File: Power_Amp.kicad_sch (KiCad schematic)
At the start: 20 parts, among them J87 Molex 73251-1153, U86 TQP7M9106

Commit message: Lots of notes and things about various items
Signed-off-by: Corey Minyard <corey@minyard.net>
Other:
- note added: "-1.3 dB"
- note added: "DC bias may affect the value of this capacitor. May need to adjust."
- note added: "Output impedance is 6.23 - j13.3 ohms This converts to 50 ohms at 435MHz"
- note added: "Place by the PA."
- note removed: "Place by the CPU."
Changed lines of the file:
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@@
 		)
 	)
-	(text "Place by the CPU."
+	(text "Place by the PA."
 		(exclude_from_sim no)
 		(at 302.514 127.254 0)
@@
 		)
 	)
+	(text "-1.3 dB"
+		(exclude_from_sim no)
+		(at 291.084 181.61 0)
+		(effects
+			(font
+				(size 1.524 1.524)
+			)
+			(justify left bottom)
+		)
+	)
 	(text "Symbol Numbers 700 up"
 		(exclude_from_sim no)
@@
 		)
 	)
+	(text "DC bias may affect the\nvalue of this capacitor.\nMay need to adjust."
+		(exclude_from_sim no)
+		(at 227.584 151.13 0)
+		(effects
+			(font
+				(size 1.524 1.524)
+			)
+		)
+	)
 	(text "Connect External 2.7 VDC supply\nhere for testing."
 		(exclude_from_sim no)
@@
 			)
 			(justify left bottom)
+		)
+	)
+	(text "Output impedance is\n6.23 - j13.3 ohms\nThis converts to 50 ohms\nat 435MHz"
+		(exclude_from_sim no)
+		(at 210.566 171.196 0)
+		(effects
+			(font
+				(size 1.524 1.524)
+			)
 		)
 	)
@@
 		(dnp no)
 		(property "Reference" "L707"
-			(at 198.12 138.43 0)
+			(at 196.342 140.97 90)
 			(effects
 				(font
@@
 		)
 		(property "Value" "18n"
-			(at 189.23 138.43 0)
-			(effects
-				(font
+			(at 191.77 140.716 90)
+			(effects
+				(font

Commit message: Add shields around AX5043s, replace UFL connectors
Signed-off-by: Corey Minyard <corey@minyard.net>
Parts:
- P701: value ~ -> CONUFL001-SMD-T; footprint PacSatDev_misc:U_FL -> PacSatDev_misc:CONN1_CONUFL_TEC
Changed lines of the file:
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@@
 			)
 		)
-		(property "Value" "~"
+		(property "Value" "CONUFL001-SMD-T"
 			(at 55.88 113.03 0)
 			(effects
@@
 					(size 1.27 1.27)
 				)
+				(hide yes)
 			)
 		)
-		(property "Footprint" "PacSatDev_misc:U_FL"
+		(property "Footprint" "PacSatDev_misc:CONN1_CONUFL_TEC"
 			(at 55.88 113.03 0)
 			(effects

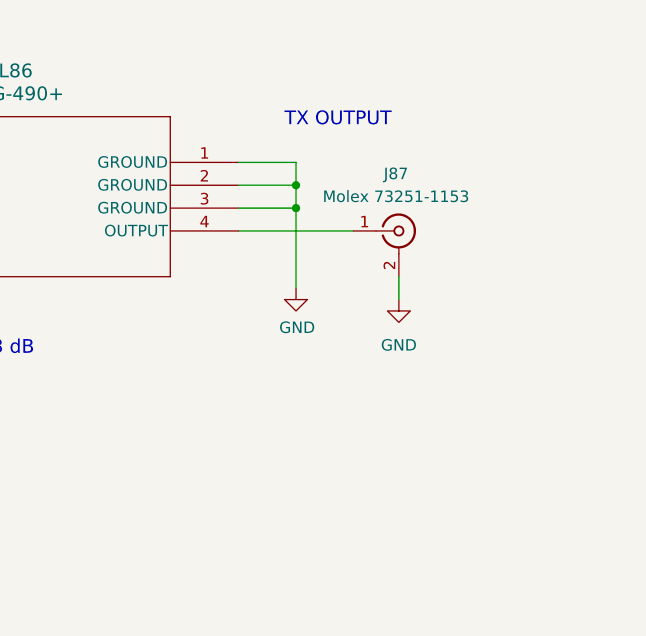
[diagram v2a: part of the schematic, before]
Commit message: Set orientaion of the shields, add bleed off inductor to TX
Signed-off-by: Corey Minyard <corey@minyard.net>
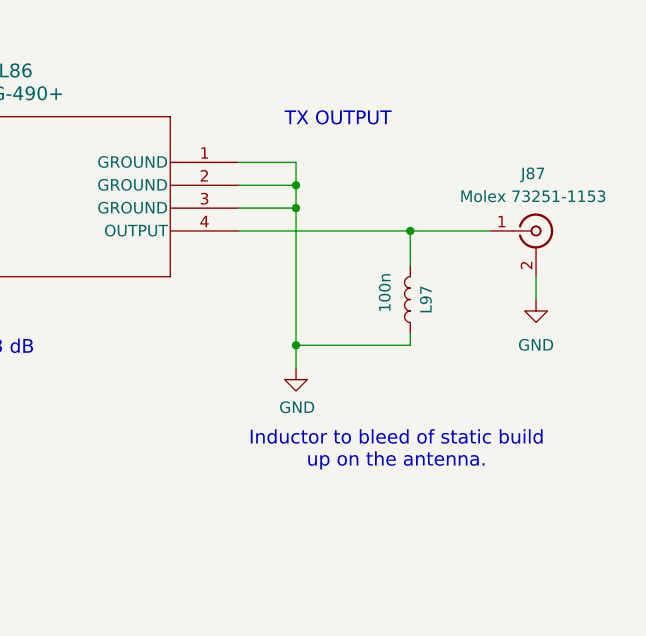
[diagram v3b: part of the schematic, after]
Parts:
- added L97: 100n, Inductor_SMD:L_0603_1608Metric_Pad1.05x0.95mm_HandSolder, symbol Device:L
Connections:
- net GND: now also L97.1
- net at FL86.4 (OUTPUT), J87.1 (In): now also L97.2
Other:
- note added: "Inductor to bleed of static build up on the antenna."
- moved on the sheet: J87
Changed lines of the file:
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@@
 		(comment 1 "N5BRG")
+	)
+	(text "Inductor to bleed of static build\nup on the antenna."
+		(exclude_from_sim no)
+		(at 338.836 192.024 0)
+		(effects
+			(font
+				(size 1.524 1.524)
+			)
+		)
 	)
 	(text "Adjust Voltage and Current for 2W"
@@
 	)
 	(junction
+		(at 327.66 180.34)
+		(diameter 0)
+		(color 0 0 0 0)
+	)
+	(junction
 		(at 147.32 149.86)
 		(diameter 0)
@@
 	)
 	(junction
+		(at 340.36 167.64)
+		(diameter 0)
+		(color 0 0 0 0)
+	)
+	(junction
 		(at 83.82 149.86)
 		(diameter 0)
@@
 	(wire
 		(pts
+			(xy 327.66 180.34) (xy 327.66 182.88)
+		)
+		(stroke
+			(width 0)
+			(type default)
+		)
+	)
+	(wire
+		(pts
 			(xy 83.82 149.86) (xy 90.17 149.86)
 		)
@@
 	(wire
 		(pts
+			(xy 340.36 180.34) (xy 327.66 180.34)
+		)
+		(stroke
+			(width 0)
+			(type default)
+		)
+	)
+	(wire
+		(pts
 			(xy 267.97 162.56) (xy 267.97 165.1)
 		)
@@
 	(wire
 		(pts
+			(xy 340.36 167.64) (xy 321.31 167.64)
+		)
+		(stroke
+			(width 0)
+			(type default)
+		)
+	)
+	(wire
+		(pts
 			(xy 194.31 116.84) (xy 194.31 128.27)
 		)
@@
 	(wire
 		(pts
-			(xy 334.01 167.64) (xy 321.31 167.64)
+			(xy 349.25 167.64) (xy 340.36 167.64)
 		)
 		(stroke
@@
 	(wire
 		(pts
-			(xy 339.09 172.72) (xy 339.09 175.26)
-		)
-		(stroke
-			(width 0)
-			(type default)
-		)
-	)
-	(wire
-		(pts
-			(xy 327.66 165.1) (xy 327.66 173.99)
+			(xy 354.33 172.72) (xy 354.33 175.26)
+		)
+		(stroke
+			(width 0)
+			(type default)
+		)
+	)
+	(wire
+		(pts
+			(xy 327.66 165.1) (xy 327.66 180.34)
 		)
 		(stroke
@@
 	(wire
 		(pts
+			(xy 340.36 167.64) (xy 340.36 171.45)
+		)
+		(stroke
+			(width 0)
+			(type default)
+		)
+	)
+	(wire
+		(pts
 			(xy 218.44 160.02) (xy 194.31 160.02)
 		)
@@
 		(pts
 			(xy 52.07 113.03) (xy 50.8 113.03)
+		)
+		(stroke
+			(width 0)
+			(type default)
+		)
+	)
+	(wire
+		(pts
+			(xy 340.36 179.07) (xy 340.36 180.34)
 		)
 		(stroke
@@
 	(symbol
 		(lib_id "Connector:Conn_Coaxial")
-		(at 339.09 167.64 0)
+		(at 354.33 167.64 0)
 		(unit 1)
 		(exclude_from_sim no)
@@
 		(fields_autoplaced yes)
 		(property "Reference" "J87"
-			(at 338.7726 161.29 0)
+			(at 354.0126 161.29 0)
 			(effects
 				(font
@@
 		)
 		(property "Value" "Molex 73251-1153"
-			(at 338.7726 163.83 0)
+			(at 354.0126 163.83 0)
 			(effects
 				(font
@@
 		)
 		(property "Footprint" "Connector_Coaxial:SMA_Molex_73251-1153_EdgeMount_Horizontal"
-			(at 339.09 167.64 0)
+			(at 354.33 167.64 0)
 			(effects
 				(font
@@
 		)
 		(property "Datasheet" "~"
-			(at 339.09 167.64 0)
+			(at 354.33 167.64 0)
 			(effects
 				(font
@@
 		)
 		(property "Description" "coaxial connector (BNC, SMA, SMB, SMC, Cinch/RCA, LEMO, ...)"
-			(at 339.09 167.64 0)
+			(at 354.33 167.64 0)
 			(effects
 				(font
@@
 	(symbol
 		(lib_id "power:GND")
-		(at 327.66 173.99 0)
+		(at 327.66 182.88 0)
 		(unit 1)
 		(exclude_from_sim no)
@@
 		(dnp no)
 		(property "Reference" "#PWR0200"
-			(at 327.66 180.34 0)
+			(at 327.66 189.23 0)
 			(effects
 				(font
@@
 		)
 		(property "Value" "GND"
-			(at 327.787 178.3842 0)
+			(at 327.787 187.2742 0)
 			(effects
 				(font
@@
 		)
 		(property "Footprint" ""
-			(at 327.66 173.99 0)
+			(at 327.66 182.88 0)
 			(effects
 				(font
@@
 		)
 		(property "Datasheet" ""
-			(at 327.66 173.99 0)
+			(at 327.66 182.88 0)
 			(effects
 				(font
@@
 		)
 		(property "Description" ""
-			(at 327.66 173.99 0)
+			(at 327.66 182.88 0)
 			(effects
 				(font
@@
 	(symbol
 		(lib_id "power:GND")
-		(at 339.09 175.26 0)
+		(at 354.33 175.26 0)
 		(mirror y)
 		(unit 1)
@@
 		(fields_autoplaced yes)
 		(property "Reference" "#PWR0191"
-			(at 339.09 181.61 0)
+			(at 354.33 181.61 0)
 			(effects
 				(font
@@
 		)
 		(property "Value" "GND"
-			(at 339.09 180.34 0)
+			(at 354.33 180.34 0)
 			(effects
 				(font
@@
 		)
 		(property "Footprint" ""
-			(at 339.09 175.26 0)
+			(at 354.33 175.26 0)
 			(effects
 				(font
@@
 		)
 		(property "Datasheet" ""
-			(at 339.09 175.26 0)
+			(at 354.33 175.26 0)
 			(effects
 				(font
@@
 		)
 		(property "Description" ""
-			(at 339.09 175.26 0)
+			(at 354.33 175.26 0)
 			(effects
 				(font
@@
 					(unit 1)
 				)
+			)
+		)
+	)
+	(symbol
+		(lib_id "Device:L")
+		(at 340.36 175.26 180)
+		(unit 1)
+		(exclude_from_sim no)
+		(in_bom yes)
+		(on_board yes)
+		(dnp no)
+		(property "Reference" "L97"
+			(at 342.138 175.26 90)
+			(effects
+				(font
+					(size 1.27 1.27)
+				)
+			)
+		)
+		(property "Value" "100n"
+			(at 337.566 174.498 90)
+			(effects
+				(font
+					(size 1.27 1.27)
+				)
+			)
+		)
+		(property "Footprint" "Inductor_SMD:L_0603_1608Metric_Pad1.05x0.95mm_HandSolder"
+			(at 340.36 175.26 0)
+			(effects
+				(font
+					(size 1.27 1.27)
+				)
+				(hide yes)
+			)
+		)
+		(property "Datasheet" "~"
+			(at 340.36 175.26 0)
+			(effects
+				(font
+					(size 1.27 1.27)
+				)
+				(hide yes)
+			)
+		)
+		(property "Description" ""
+			(at 340.36 175.26 0)
+			(effects
+				(font
+					(size 1.27 1.27)
+				)
+			)
+		)
+		(pin "1"
+		)
+		(pin "2"
+		)
+		(instances
+			(project "PacSat_AFSK"
+				(path "/cc9f42d2-6985-41ac-acab-5ab7b01c5b38/b85b88c3-87c5-49e2-804e-0759552ace3d"
+					(reference "L97")
+					(unit 1)
+				)

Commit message: Rework the AX5043 RX side to a different balun
It's cheaper (though not smaller) and fits inside the shield.

Signed-off-by: Corey Minyard <corey@minyard.net>
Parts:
- removed R133: 0, Resistor_SMD:R_0603_1608Metric_Pad0.98x0.95mm_HandSolder, symbol Device:R
- added C137: 100p, Capacitor_SMD:C_0603_1608Metric_Pad1.08x0.95mm_HandSolder, symbol Device:C
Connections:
- net TX_OUT_DRV: now also C137.1
- net at C708.1, L706.1, P701.1 (In): now also C137.2
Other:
- note removed: "Adjust Voltage and Current for 2W"
- note removed: "Connect External 2.7 VDC supply here for testing."
- note removed: "RF Shield over these parts."
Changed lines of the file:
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@@
 		)
 	)
-	(text "Adjust Voltage and Current for 2W"
-		(exclude_from_sim no)
-		(at 119.38 59.69 0)
-		(effects
-			(font
-				(size 1.524 1.524)
-			)
-			(justify right bottom)
-		)
-	)
 	(text "Place by the PA."
 		(exclude_from_sim no)
@@
 		)
 	)
-	(text "RF Shield over these parts."
-		(exclude_from_sim no)
-		(at 31.75 186.69 0)
-		(effects
-			(font
-				(size 1.524 1.524)
-			)
-			(justify left bottom)
-		)
-	)
 	(text "33 dBm\n2 W"
 		(exclude_from_sim no)
@@
 		)
 	)
-	(text "Connect External 2.7 VDC supply\nhere for testing."
-		(exclude_from_sim no)
-		(at 153.67 40.64 0)
-		(effects
-			(font
-				(size 1.524 1.524)
-			)
-			(justify right bottom)
-		)
-	)
 	(text "Input impedance is\n1.87 - 37.7j this\nmatches to 50 ohms\nat 435MHz."
 		(exclude_from_sim no)
@@
 	)
 	(symbol
-		(lib_id "Device:R")
-		(at 45.72 142.24 90)
-		(unit 1)
-		(exclude_from_sim no)
-		(in_bom yes)
-		(on_board yes)
-		(dnp no)
-		(fields_autoplaced yes)
-		(property "Reference" "R133"
-			(at 45.72 135.89 90)
-			(effects
-				(font
-					(size 1.27 1.27)
-				)
-			)
-		)
-		(property "Value" "0"
-			(at 45.72 138.43 90)
-			(effects
-				(font
-					(size 1.27 1.27)
-				)
-			)
-		)
-		(property "Footprint" "Resistor_SMD:R_0603_1608Metric_Pad0.98x0.95mm_HandSolder"
-			(at 45.72 144.018 90)
-			(effects
-				(font
-					(size 1.27 1.27)
-				)
-				(hide yes)
-			)
-		)
-		(property "Datasheet" "~"
-			(at 45.72 142.24 0)
-			(effects
-				(font
-					(size 1.27 1.27)
-				)
-				(hide yes)
-			)
-		)
-		(property "Description" ""
-			(at 45.72 142.24 0)
-			(effects
-				(font
-					(size 1.27 1.27)
-				)
-			)
-		)
-		(pin "1"
-		)
-		(pin "2"
-		)
-		(instances
-			(project "PacSat_AFSK"
-				(path "/cc9f42d2-6985-41ac-acab-5ab7b01c5b38/b85b88c3-87c5-49e2-804e-0759552ace3d"
-					(reference "R133")
-					(unit 1)
-				)
-			)
-		)
-	)
-	(symbol
 		(lib_id "power:GND")
 		(at 327.66 182.88 0)
@@
 					(unit 1)
 				)
+			)
+		)
+	)
+	(symbol
+		(lib_id "Device:C")
+		(at 45.72 142.24 90)
+		(mirror x)
+		(unit 1)
+		(exclude_from_sim no)
+		(in_bom yes)
+		(on_board yes)
+		(dnp no)
+		(property "Reference" "C137"
+			(at 45.72 135.89 90)
+			(effects
+				(font
+					(size 1.27 1.27)
+				)
+			)
+		)
+		(property "Value" "100p"
+			(at 45.72 138.43 90)
+			(effects
+				(font
+					(size 1.27 1.27)
+				)
+			)
+		)
+		(property "Footprint" "Capacitor_SMD:C_0603_1608Metric_Pad1.08x0.95mm_HandSolder"
+			(at 49.53 143.2052 0)
+			(effects
+				(font
+					(size 1.27 1.27)
+				)
+				(hide yes)
+			)
+		)
+		(property "Datasheet" "~"
+			(at 45.72 142.24 0)
+			(effects
+				(font
+					(size 1.27 1.27)
+				)
+				(hide yes)
+			)
+		)
+		(property "Description" ""
+			(at 45.72 142.24 0)
+			(effects
+				(font
+					(size 1.27 1.27)
+				)
+			)
+		)
+		(pin "1"
+		)
+		(pin "2"
+		)
+		(instances
+			(project "PacSat_AFSK"
+				(path "/cc9f42d2-6985-41ac-acab-5ab7b01c5b38/b85b88c3-87c5-49e2-804e-0759552ace3d"
+					(reference "C137")
+					(unit 1)
+				)

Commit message: Add shield for the TX PA section
Signed-off-by: Corey Minyard <corey@minyard.net>
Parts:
- added J94: PIC-S-203F, PacSatDev_misc:RF_SHIELD_PIC_S_203, symbol Device:RFShield_OnePiece
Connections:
- net GND: now also J94.1 (Shield)
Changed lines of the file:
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@@
+	(wire
+		(pts
+			(xy 105.41 58.42) (xy 105.41 60.96)
+		)
+		(stroke
+			(width 0)
+			(type default)
+		)
+	)
 	(wire
 		(pts
@@
 				(path "/cc9f42d2-6985-41ac-acab-5ab7b01c5b38/b85b88c3-87c5-49e2-804e-0759552ace3d"
 					(reference "P701")
+					(unit 1)
+				)
+			)
+		)
+	)
+	(symbol
+		(lib_id "Device:RFShield_OnePiece")
+		(at 105.41 48.26 0)
+		(unit 1)
+		(exclude_from_sim no)
+		(in_bom yes)
+		(on_board yes)
+		(dnp no)
+		(fields_autoplaced yes)
+		(property "Reference" "J94"
+			(at 121.92 46.9899 0)
+			(effects
+				(font
+					(size 1.27 1.27)
+				)
+				(justify left)
+			)
+		)
+		(property "Value" "PIC-S-203F"
+			(at 121.92 49.5299 0)
+			(effects
+				(font
+					(size 1.27 1.27)
+				)
+				(justify left)
+			)
+		)
+		(property "Footprint" "PacSatDev_misc:RF_SHIELD_PIC_S_203"
+			(at 105.41 50.8 0)
+			(effects
+				(font
+					(size 1.27 1.27)
+				)
+				(hide yes)
+			)
+		)
+		(property "Datasheet" "~"
+			(at 105.41 50.8 0)
+			(effects
+				(font
+					(size 1.27 1.27)
+				)
+				(hide yes)
+			)
+		)
+		(property "Description" "One-piece EMI RF shielding cabinet"
+			(at 105.41 48.26 0)
+			(effects
+				(font
+					(size 1.27 1.27)
+				)
+				(hide yes)
+			)
+		)
+		(pin "1"
+		)
+		(instances
+			(project "PacSat_AFSK"
+				(path "/cc9f42d2-6985-41ac-acab-5ab7b01c5b38/b85b88c3-87c5-49e2-804e-0759552ace3d"
+					(reference "J94")
 					(unit 1)
 				)
@@
 					(unit 1)
 				)
+			)
+		)
+	)
+	(symbol
+		(lib_id "power:GND")
+		(at 105.41 60.96 0)
+		(unit 1)
+		(exclude_from_sim no)
+		(in_bom yes)
+		(on_board yes)
+		(dnp no)
+		(fields_autoplaced yes)
+		(property "Reference" "#PWR0222"
+			(at 105.41 67.31 0)
+			(effects
+				(font
+					(size 1.27 1.27)
+				)
+				(hide yes)
+			)
+		)
+		(property "Value" "GND"
+			(at 105.41 66.04 0)
+			(effects
+				(font
+					(size 1.27 1.27)
+				)
+			)
+		)
+		(property "Footprint" ""
+			(at 105.41 60.96 0)
+			(effects
+				(font
+					(size 1.27 1.27)
+				)
+				(hide yes)
+			)
+		)
+		(property "Datasheet" ""
+			(at 105.41 60.96 0)
+			(effects
+				(font
+					(size 1.27 1.27)
+				)
+				(hide yes)
+			)
+		)
+		(property "Description" ""
+			(at 105.41 60.96 0)
+			(effects
+				(font
+					(size 1.27 1.27)
+				)
+			)
+		)
+		(pin "1"
+		)
+		(instances
+			(project "PacSat_AFSK"
+				(path "/cc9f42d2-6985-41ac-acab-5ab7b01c5b38/b85b88c3-87c5-49e2-804e-0759552ace3d"
+					(reference "#PWR0222")
+					(unit 1)
+				)

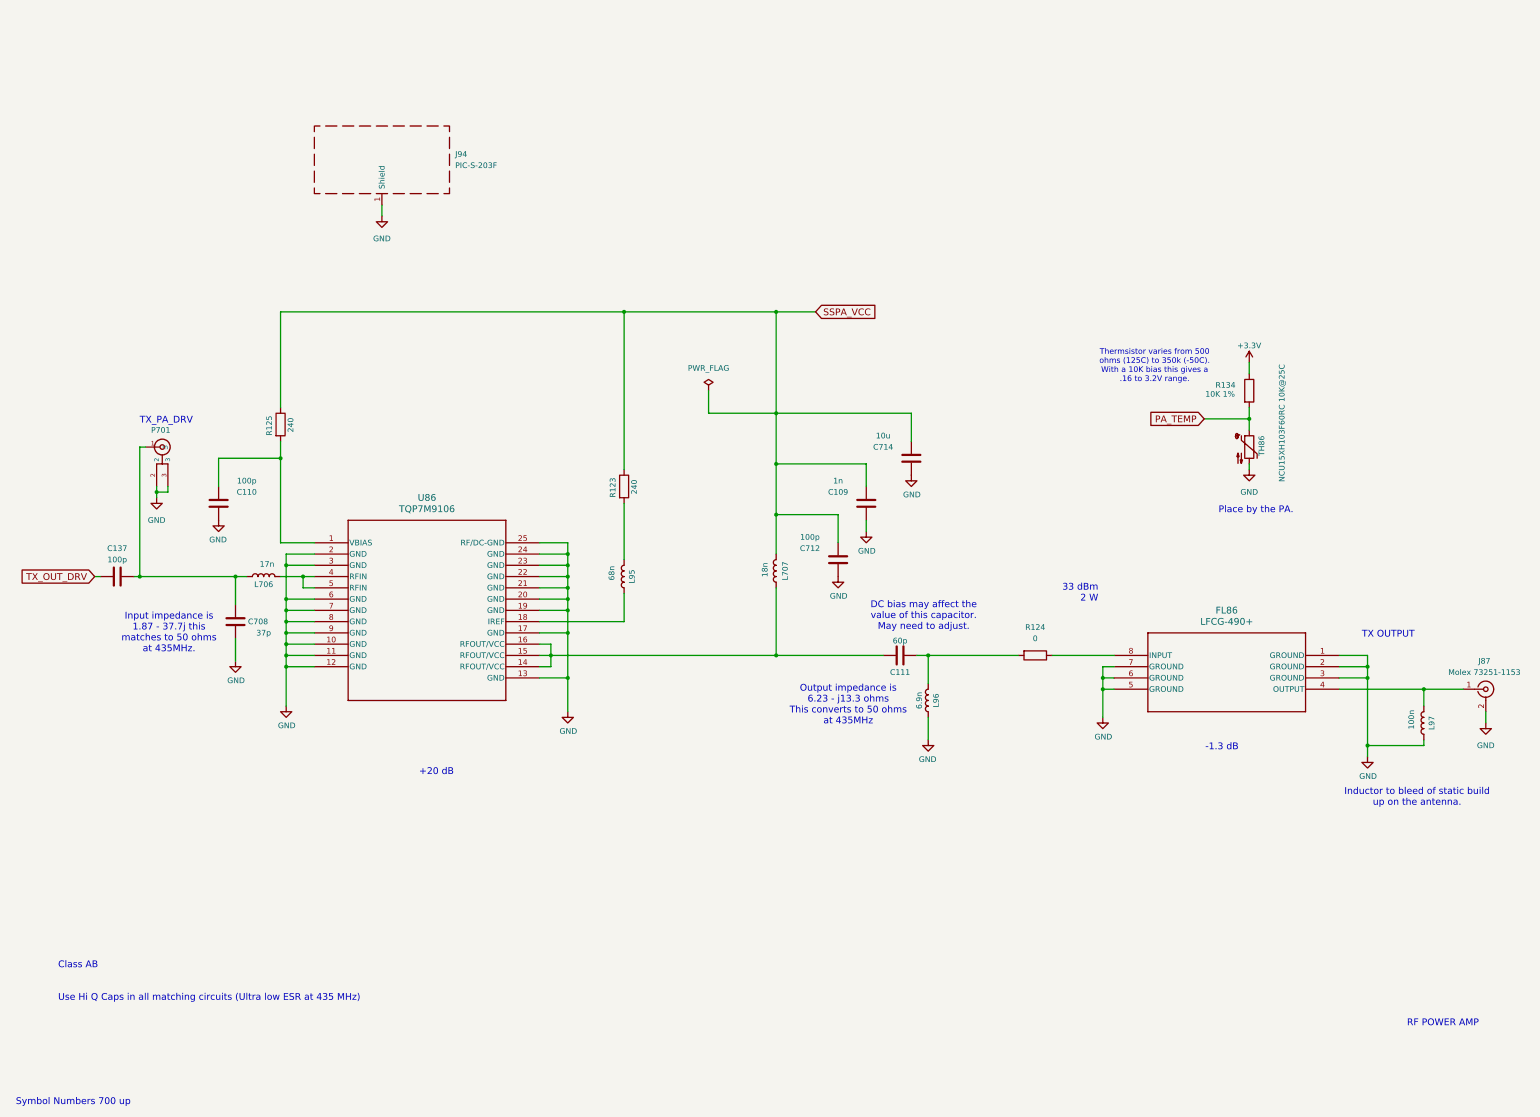
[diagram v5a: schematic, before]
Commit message: Re-annotate all parts
And get rid of the per-sheet annotation remarks.

Signed-off-by: Corey Minyard <corey@minyard.net>
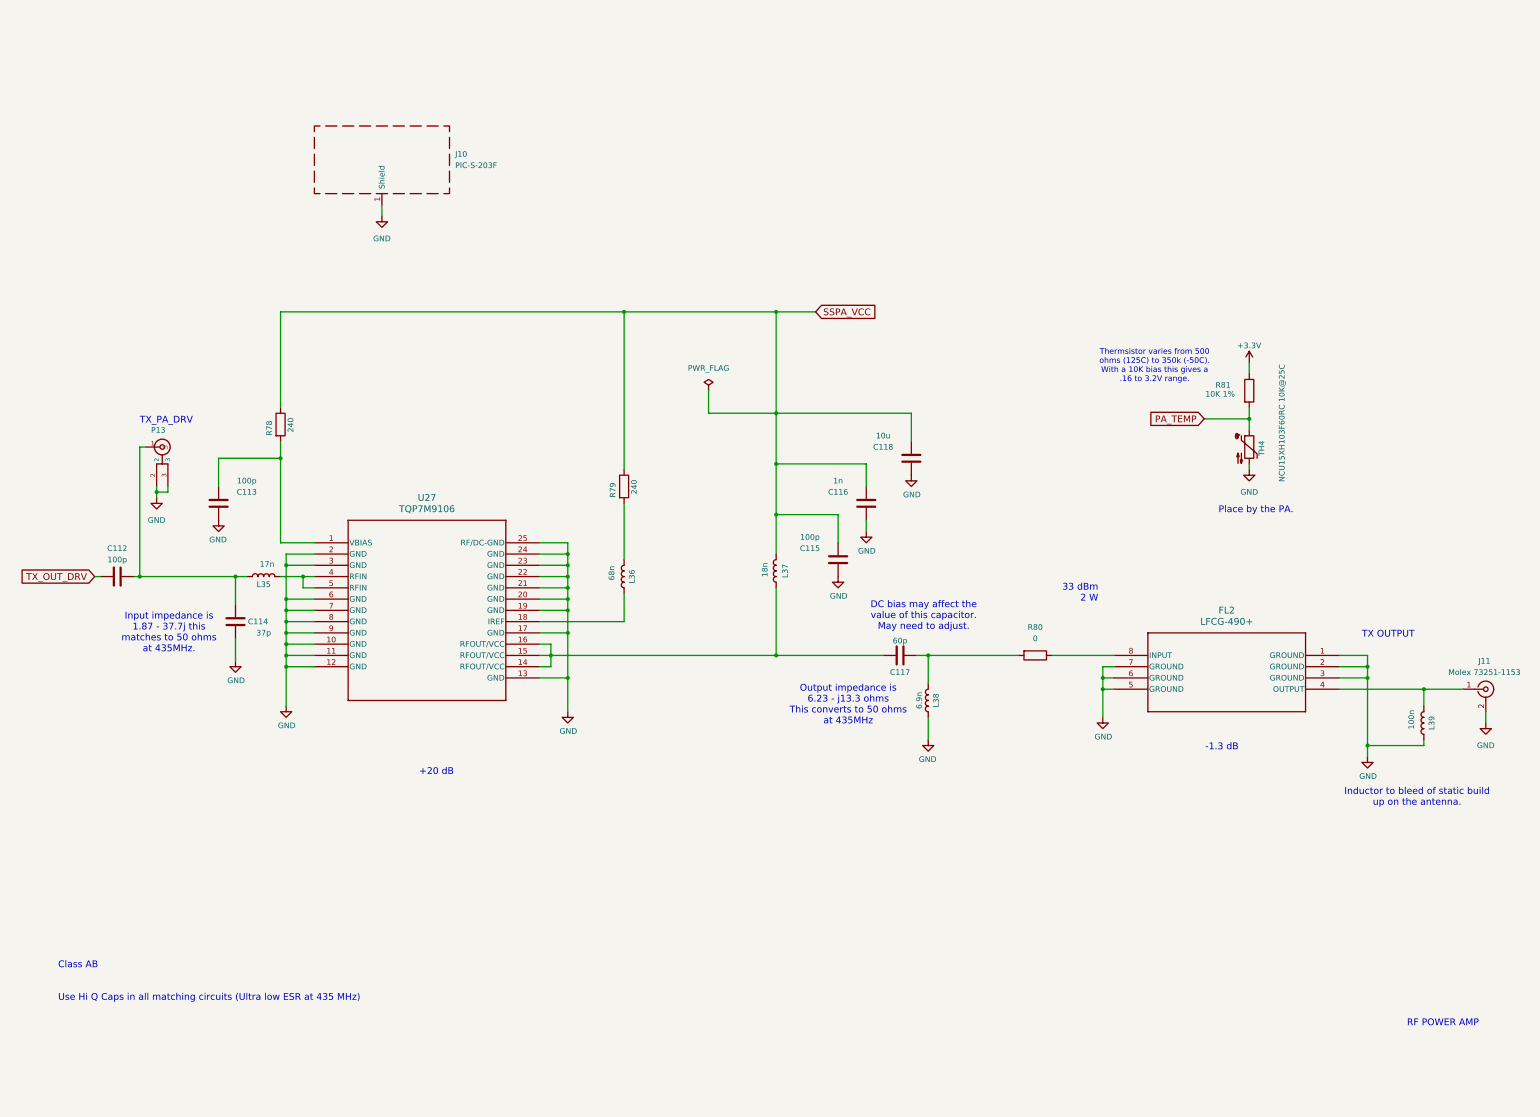
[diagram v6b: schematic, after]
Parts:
- renumbered C137 to C112, C110 to C113, C708 to C114, C712 to C115, C109 to C116, C111 to C117, C714 to C118, FL86 to FL2, J94 to J10, J87 to J11, L706 to L35, L95 to L36, L707 to L37, L96 to L38, L97 to L39, P701 to P13, R125 to R78, R123 to R79, R124 to R80, R134 to R81, TH86 to TH4, U86 to U27
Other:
- note removed: "Symbol Numbers 700 up"
